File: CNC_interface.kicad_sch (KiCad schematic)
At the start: 25 parts, among them J1 Conn_01x04_Male, J10 Conn_01x08, J11 Conn_01x08, J12 Conn_01x08, J13 Conn_01x08, J14 Conn_01x03_Male, J15 Conn_01x03_Male, J16 Conn_01x03_Male, J17 Conn_01x08, J18 Conn_01x10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

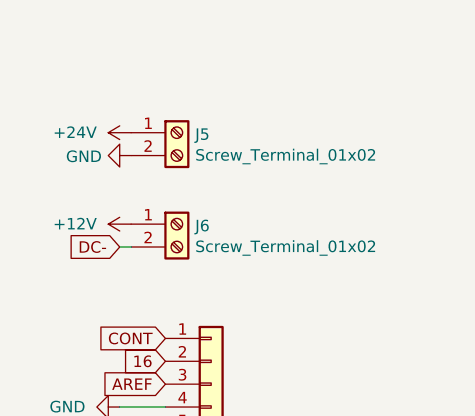
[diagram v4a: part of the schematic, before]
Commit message: place components
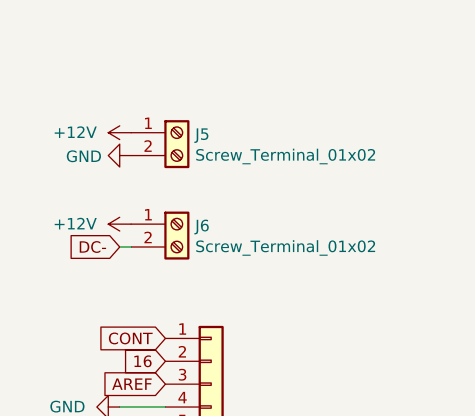
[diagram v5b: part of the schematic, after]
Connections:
- net +24V is gone; now on net +12V: J5.1 (Pin_1)
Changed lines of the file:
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@@
   (symbol (lib_id "power:+12V") (at 148.59 82.55 90) (unit 1)
     (in_bom yes) (on_board yes) (fields_autoplaced)
-    (property "Reference" "#PWR?" (id 0) (at 152.4 82.55 0)
+    (property "Reference" "#PWR0133" (id 0) (at 152.4 82.55 0)
       (effects (font (size 1.27 1.27)) hide)
     )
@@
     (pin "2")
   )
-  (symbol (lib_id "power:+24V") (at 41.91 31.75 90) (unit 1)
-    (in_bom yes) (on_board yes) (fields_autoplaced)
-    (property "Reference" "#PWR0120" (id 0) (at 45.72 31.75 0)
-      (effects (font (size 1.27 1.27)) hide)
-    )
-    (property "Value" "+24V" (id 1) (at 38.1 31.7499 90)
+  (symbol (lib_id "power:+12V") (at 41.91 31.75 90) (unit 1)
+    (in_bom yes) (on_board yes) (fields_autoplaced)
+    (property "Reference" "#PWR?" (id 0) (at 45.72 31.75 0)
+      (effects (font (size 1.27 1.27)) hide)
+    )
+    (property "Value" "+12V" (id 1) (at 38.1 31.7499 90)
       (effects (font (size 1.27 1.27)) (justify left))
     )
@@
   (symbol (lib_id "power:+12V") (at 148.59 50.8 90) (unit 1)
     (in_bom yes) (on_board yes) (fields_autoplaced)
-    (property "Reference" "#PWR?" (id 0) (at 152.4 50.8 0)
+    (property "Reference" "#PWR0136" (id 0) (at 152.4 50.8 0)
       (effects (font (size 1.27 1.27)) hide)
     )
@@
   (symbol (lib_id "power:+12V") (at 148.59 114.3 90) (unit 1)
     (in_bom yes) (on_board yes) (fields_autoplaced)
-    (property "Reference" "#PWR?" (id 0) (at 152.4 114.3 0)
+    (property "Reference" "#PWR0132" (id 0) (at 152.4 114.3 0)
       (effects (font (size 1.27 1.27)) hide)
     )
@@
       (reference "#PWR0119") (unit 1) (value "+12V") (footprint "")
     )
-    (path "/7fee173e-94bd-42a9-8a7e-cd76998ba180"
-      (reference "#PWR0120") (unit 1) (value "+24V") (footprint "")
-    )
     (path "/00000000-0000-0000-0000-0000620756d9"
       (reference "#PWR0121") (unit 1) (value "GND") (footprint "")
@@
       (reference "#PWR0125") (unit 1) (value "GND") (footprint "")
     )
-    (path "/8b7d305c-caee-4338-94fc-4790d784af7f/4fb30122-c579-4c23-b56d-ffd6ad498666"
-      (reference "#PWR0126") (unit 1) (value "+24V") (footprint "")
-    )
     (path "/8b7d305c-caee-4338-94fc-4790d784af7f/f716deb6-15eb-49bb-86b7-7e00537a8574"
       (reference "#PWR0127") (unit 1) (value "+5V") (footprint "")
     )
-    (path "/8b7d305c-caee-4338-94fc-4790d784af7f/bbb066ba-6a5d-4725-9642-d6966dbc996c"
-      (reference "#PWR0128") (unit 1) (value "GND") (footprint "")
-    )
-    (path "/8b7d305c-caee-4338-94fc-4790d784af7f/7177e43a-75cb-46af-b7a6-2cc7ae98573e"
-      (reference "#PWR0129") (unit 1) (value "GND") (footprint "")
-    )
-    (path "/8b7d305c-caee-4338-94fc-4790d784af7f/02ec1a19-47b3-40f2-a6c0-99c0c27f9573"
-      (reference "#PWR0130") (unit 1) (value "+24V") (footprint "")
-    )
     (path "/e42d9733-e287-4e19-b1d1-7f9d7fbba791"
       (reference "#PWR0131") (unit 1) (value "+5V") (footprint "")
     )
+    (path "/ba652f01-eff8-486a-ad05-0601e550fdde"
+      (reference "#PWR0132") (unit 1) (value "+12V") (footprint "")
+    )
+    (path "/306356ce-3d3d-4ee4-ab88-99af3cfd3700"
+      (reference "#PWR0133") (unit 1) (value "+12V") (footprint "")
+    )
     (path "/9cc3fedb-e7e4-4d83-84e3-7ed5b13ae7b5"
       (reference "#PWR0134") (unit 1) (value "+5V") (footprint "")
@@
       (reference "#PWR0135") (unit 1) (value "+5V") (footprint "")
     )
+    (path "/998f8fc2-f876-46d4-9582-c9487fcb3793"
+      (reference "#PWR0136") (unit 1) (value "+12V") (footprint "")
+    )
     (path "/8b7d305c-caee-4338-94fc-4790d784af7f/2ac1aff8-0f18-45cf-83e1-f1a00fd60e7c"
       (reference "#PWR0137") (unit 1) (value "GND") (footprint "")
@@
       (reference "#PWR0140") (unit 1) (value "GND") (footprint "")
     )
-    (path "/8b7d305c-caee-4338-94fc-4790d784af7f/a58ff555-40af-49a5-aeec-82862584bd28"
-      (reference "#PWR0141") (unit 1) (value "GND") (footprint "")
-    )
-    (path "/8b7d305c-caee-4338-94fc-4790d784af7f/b91be5e0-c296-47a9-9332-4afbd2ae0eb7"
-      (reference "#PWR0142") (unit 1) (value "GND") (footprint "")
-    )
-    (path "/8b7d305c-caee-4338-94fc-4790d784af7f/3ecdde75-e876-4968-8795-4c5c3548fa6b"
-      (reference "#PWR0143") (unit 1) (value "+12V") (footprint "")
-    )
-    (path "/8b7d305c-caee-4338-94fc-4790d784af7f/389c7f73-8025-44ff-baa7-f0848bb8d9ec"
-      (reference "#PWR0144") (unit 1) (value "GND") (footprint "")
-    )
     (path "/1a9ee27d-22cb-44eb-bb67-3f13b74866fa"
       (reference "#PWR0145") (unit 1) (value "+5V") (footprint "")
@@
       (reference "#PWR0147") (unit 1) (value "GND") (footprint "")
     )
-    (path "/306356ce-3d3d-4ee4-ab88-99af3cfd3700"
+    (path "/87170310-6dd0-4dd4-8af1-99e2c852efea"
       (reference "#PWR?") (unit 1) (value "+12V") (footprint "")
     )
-    (path "/998f8fc2-f876-46d4-9582-c9487fcb3793"
-      (reference "#PWR?") (unit 1) (value "+12V") (footprint "")
-    )
-    (path "/ba652f01-eff8-486a-ad05-0601e550fdde"
+    (path "/8b7d305c-caee-4338-94fc-4790d784af7f/93fc451d-eabf-4885-ab8e-7534bc42943c"
       (reference "#PWR?") (unit 1) (value "+12V") (footprint "")
     )
@@
       (reference "C5") (unit 1) (value "100uF") (footprint "Capacitor_THT:CP_Radial_D6.3mm_P2.50mm")
     )
-    (path "/8b7d305c-caee-4338-94fc-4790d784af7f/38e766e3-8f0d-435f-85a7-b841375c9d0e"
-      (reference "C6") (unit 1) (value "100µF") (footprint "Capacitor_THT:CP_Radial_D6.3mm_P2.50mm")
-    )
-    (path "/8b7d305c-caee-4338-94fc-4790d784af7f/7f0debda-8e70-4f6a-ab19-a22319396f56"
-      (reference "C7") (unit 1) (value "1000µF") (footprint "Capacitor_THT:CP_Radial_D12.5mm_P5.00mm")
-    )
     (path "/00000000-0000-0000-0000-000062073139"
       (reference "D1") (unit 1) (value "1N4001") (footprint "Diode_THT:D_DO-41_SOD81_P10.16mm_Horizontal")
@@
       (reference "D2") (unit 1) (value "1N5822") (footprint "Diode_THT:D_DO-201AD_P15.24mm_Horizontal")
     )
-    (path "/8b7d305c-caee-4338-94fc-4790d784af7f/7b5afcba-dd6f-4e98-9096-c351a002b7c2"
-      (reference "D3") (unit 1) (value "1N5822") (footprint "Diode_THT:D_DO-201AD_P15.24mm_Horizontal")
-    )
     (path "/00000000-0000-0000-0000-000062062d4c"
       (reference "J1") (unit 1) (value "Conn_01x04_Male") (footprint "Connector_JST:JST_XH_B4B-XH-A_1x04_P2.50mm_Vertical")
@@
       (reference "L1") (unit 1) (value "150µF") (footprint "CNC_interface:L_Radial_24.4mm_P23.50mm_Murata_1400series")
     )
-    (path "/8b7d305c-caee-4338-94fc-4790d784af7f/6ef44ea8-e69c-45bc-be4d-863f0548e8f5"
-      (reference "L2") (unit 1) (value "220µH") (footprint "CNC_interface:L_Radial_24.4mm_P23.50mm_Murata_1400series")
-    )
     (path "/00000000-0000-0000-0000-000062070cd9"
       (reference "Q1") (unit 1) (value "Q_NMOS_GDS") (footprint "Package_TO_SOT_THT:TO-220-3_Vertical")
@@
       (reference "U1") (unit 1) (value "LM2576HVT-5") (footprint "Package_TO_SOT_THT:TO-220-5_Vertical")
     )
-    (path "/8b7d305c-caee-4338-94fc-4790d784af7f/5db8c8eb-fb9e-454a-ae6c-6f94be11fb8d"
-      (reference "U2") (unit 1) (value "LM2576HVT-12") (footprint "Package_TO_SOT_THT:TO-220-5_Vertical")
-    )
-  )
+  )
